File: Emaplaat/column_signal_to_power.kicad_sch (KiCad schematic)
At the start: 56 parts, among them IC3 1EDN7550BXTSA1, IC41 1EDN7550BXTSA1, IC42 1EDN7550BXTSA1, IC43 1EDN7550BXTSA1, IC44 1EDN7550BXTSA1, IC45 1EDN7550BXTSA1, IC46 1EDN7550BXTSA1, IC47 1EDN7550BXTSA1, IC48 1EDN7550BXTSA1, IC49 1EDN7550BXTSA1, IC50 1EDN7550BXTSA1, IC51 1EDN7550BXTSA1, IC52 1EDN7550BXTSA1, IC53 1EDN7550BXTSA1

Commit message: jajald
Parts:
- removed C41, C42, C49, C50, C51, C52, C53, C54, C55, C56, C57, C58: 100u, Capacitor_SMD:C_0201_0603Metric_Pad0.64x0.40mm_HandSolder, symbol Device:C
- added C28, C29, C30, C31, C32, C33, C34, C35, C36, C37, C38, C39: 100u, Capacitor_SMD:C_0603_1608Metric_Pad1.08x0.95mm_HandSolder, symbol Device:C
- C27: renamed from C10; footprint Capacitor_SMD:C_0201_0603Metric_Pad0.64x0.40mm_HandSolder -> Capacitor_SMD:C_0603_1608Metric_Pad1.08x0.95mm_HandSolder
- C40: footprint Capacitor_SMD:C_0201_0603Metric_Pad0.64x0.40mm_HandSolder -> Capacitor_SMD:C_0603_1608Metric_Pad1.08x0.95mm_HandSolder
- renumbered IC3 to IC18, IC44 to IC19, IC50 to IC20, IC41 to IC21, IC45 to IC22, IC51 to IC23, IC42 to IC24, IC46 to IC25, IC52 to IC26, IC43 to IC27, IC48 to IC28, IC53 to IC29, IC47 to IC30, IC49 to IC31, R6 to R27, R64 to R28, R76 to R29, R7 to R30, R65 to R31, R77 to R32, R58 to R33, R66 to R34, R78 to R35, R59 to R36, R67 to R37, R79 to R38, R60 to R39, R68 to R40, R80 to R41, R61 to R42, R69 to R43, R81 to R44, R62 to R45, R72 to R46, R82 to R47, R63 to R48, R73 to R49, R83 to R50, R70 to R51, R74 to R52, R71 to R53, R75 to R54
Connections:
- net 12V: now also C28.2, C29.2, C30.2, C31.2, C32.2, C33.2, C34.2, C35.2, C36.2, C37.2, C38.2, C39.2
- net GND: now also C28.1, C29.1, C30.1, C31.1, C32.1, C33.1, C34.1, C35.1, C36.1, C37.1, C38.1, C39.1

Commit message: skeem korras
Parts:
- IC18, IC19, IC20, IC21, IC22, IC23, IC24, IC25, IC26, IC27, IC28, IC29, IC30, IC31: footprint SOT95P280X145-6N -> SOT95P280X145-6N:SOT95P280X145-6N
- renumbered C36 to C28, C37 to C29, C28 to C30, C35 to C31, C38 to C32, C29 to C33, C39 to C35, C30 to C36, C33 to C37, C40 to C38, C31 to C39, C32 to C40
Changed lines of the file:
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@@
 			)
 		)
-		(property "Footprint" "SOT95P280X145-6N"
+		(property "Footprint" "SOT95P280X145-6N:SOT95P280X145-6N"
 			(at 73.66 258.75 0)
 			(effects
@@
 			)
 		)
-		(property "Footprint" "SOT95P280X145-6N"
+		(property "Footprint" "SOT95P280X145-6N:SOT95P280X145-6N"
 			(at 163.83 126.67 0)
 			(effects
@@
 			)
 		)
-		(property "Footprint" "SOT95P280X145-6N"
+		(property "Footprint" "SOT95P280X145-6N:SOT95P280X145-6N"
 			(at 250.19 229.54 0)
 			(effects
@@
 			)
 		)
-		(property "Footprint" "SOT95P280X145-6N"
+		(property "Footprint" "SOT95P280X145-6N:SOT95P280X145-6N"
 			(at 162.56 162.23 0)
 			(effects
@@
 			)
 		)
-		(property "Footprint" "SOT95P280X145-6N"
+		(property "Footprint" "SOT95P280X145-6N:SOT95P280X145-6N"
 			(at 162.56 228.27 0)
 			(effects
@@
 			)
 		)
-		(property "Footprint" "SOT95P280X145-6N"
+		(property "Footprint" "SOT95P280X145-6N:SOT95P280X145-6N"
 			(at 250.19 196.52 0)
 			(effects
@@
 		(on_board yes)
 		(dnp no)
-		(property "Reference" "C40"
+		(property "Reference" "C38"
 			(at 215.265 143.51 0)
 			(effects
@@
 			(project "Emaplaat"
 				(path "/489224c0-ace1-4530-aa61-a5d03adf1434/1d123e2b-7c0a-4548-ab70-18ecbd0f3e35/07a510d3-c099-46a7-9717-c70cc79e70f4"
-					(reference "C40")
+					(reference "C38")
 					(unit 1)
 				)
@@
 		(on_board yes)
 		(dnp no)
-		(property "Reference" "C37"
+		(property "Reference" "C29"
 			(at 216.535 41.91 0)
 			(effects
@@
 			(project "Emaplaat"
 				(path "/489224c0-ace1-4530-aa61-a5d03adf1434/1d123e2b-7c0a-4548-ab70-18ecbd0f3e35/07a510d3-c099-46a7-9717-c70cc79e70f4"
-					(reference "C37")
+					(reference "C29")
 					(unit 1)
 				)
@@
 		(on_board yes)
 		(dnp no)
-		(property "Reference" "C35"
+		(property "Reference" "C31"
 			(at 127.635 76.2 0)
 			(effects
@@
 			(project "Emaplaat"
 				(path "/489224c0-ace1-4530-aa61-a5d03adf1434/1d123e2b-7c0a-4548-ab70-18ecbd0f3e35/07a510d3-c099-46a7-9717-c70cc79e70f4"
-					(reference "C35")
+					(reference "C31")
 					(unit 1)
 				)
@@
 			)
 		)
-		(property "Footprint" "SOT95P280X145-6N"
+		(property "Footprint" "SOT95P280X145-6N:SOT95P280X145-6N"
 			(at 73.66 191.44 0)
 			(effects
@@
 		(on_board yes)
 		(dnp no)
-		(property "Reference" "C31"
+		(property "Reference" "C39"
 			(at 38.735 172.72 0)
 			(effects
@@
 			(project "Emaplaat"
 				(path "/489224c0-ace1-4530-aa61-a5d03adf1434/1d123e2b-7c0a-4548-ab70-18ecbd0f3e35/07a510d3-c099-46a7-9717-c70cc79e70f4"
-					(reference "C31")
+					(reference "C39")
 					(unit 1)
 				)
@@
 		(on_board yes)
 		(dnp no)
-		(property "Reference" "C38"
+		(property "Reference" "C32"
 			(at 215.265 77.47 0)
 			(effects
@@
 			(project "Emaplaat"
 				(path "/489224c0-ace1-4530-aa61-a5d03adf1434/1d123e2b-7c0a-4548-ab70-18ecbd0f3e35/07a510d3-c099-46a7-9717-c70cc79e70f4"
-					(reference "C38")
+					(reference "C32")
 					(unit 1)
 				)
@@
 			)
 		)
-		(property "Footprint" "SOT95P280X145-6N"
+		(property "Footprint" "SOT95P280X145-6N:SOT95P280X145-6N"
 			(at 162.56 262.56 0)
 			(effects
@@
 		(on_board yes)
 		(dnp no)
-		(property "Reference" "C28"
+		(property "Reference" "C30"
 			(at 38.735 72.39 0)
 			(effects
@@
 			(project "Emaplaat"
 				(path "/489224c0-ace1-4530-aa61-a5d03adf1434/1d123e2b-7c0a-4548-ab70-18ecbd0f3e35/07a510d3-c099-46a7-9717-c70cc79e70f4"
-					(reference "C28")
+					(reference "C30")
 					(unit 1)
 				)
@@
 		(on_board yes)
 		(dnp no)
-		(property "Reference" "C29"
+		(property "Reference" "C33"
 			(at 38.735 105.41 0)
 			(effects
@@
 			(project "Emaplaat"
 				(path "/489224c0-ace1-4530-aa61-a5d03adf1434/1d123e2b-7c0a-4548-ab70-18ecbd0f3e35/07a510d3-c099-46a7-9717-c70cc79e70f4"
-					(reference "C29")
+					(reference "C33")
 					(unit 1)
 				)
@@
 			)
 		)
-		(property "Footprint" "SOT95P280X145-6N"
+		(property "Footprint" "SOT95P280X145-6N:SOT95P280X145-6N"
 			(at 162.56 195.25 0)
 			(effects
@@
 		(on_board yes)
 		(dnp no)
-		(property "Reference" "C39"
+		(property "Reference" "C35"
 			(at 215.265 110.49 0)
 			(effects
@@
 			(project "Emaplaat"
 				(path "/489224c0-ace1-4530-aa61-a5d03adf1434/1d123e2b-7c0a-4548-ab70-18ecbd0f3e35/07a510d3-c099-46a7-9717-c70cc79e70f4"
-					(reference "C39")
+					(reference "C35")
 					(unit 1)
 				)
@@
 			)
 		)
-		(property "Footprint" "SOT95P280X145-6N"
+		(property "Footprint" "SOT95P280X145-6N:SOT95P280X145-6N"
 			(at 73.66 224.46 0)
 			(effects
@@
 			)
 		)
-		(property "Footprint" "SOT95P280X145-6N"
+		(property "Footprint" "SOT95P280X145-6N:SOT95P280X145-6N"
 			(at 250.19 163.5 0)
 			(effects
@@
 		(on_board yes)
 		(dnp no)
-		(property "Reference" "C33"
+		(property "Reference" "C37"
 			(at 127.635 142.24 0)
 			(effects
@@
 			(project "Emaplaat"
 				(path "/489224c0-ace1-4530-aa61-a5d03adf1434/1d123e2b-7c0a-4548-ab70-18ecbd0f3e35/07a510d3-c099-46a7-9717-c70cc79e70f4"
-					(reference "C33")
+					(reference "C37")
 					(unit 1)
 				)
@@
 		(on_board yes)
 		(dnp no)
-		(property "Reference" "C36"
+		(property "Reference" "C28"
 			(at 129.0823 40.64 0)
 			(effects
@@
 			(project "Emaplaat"
 				(path "/489224c0-ace1-4530-aa61-a5d03adf1434/1d123e2b-7c0a-4548-ab70-18ecbd0f3e35/07a510d3-c099-46a7-9717-c70cc79e70f4"
-					(reference "C36")
+					(reference "C28")
 					(unit 1)
 				)
@@
 			)
 		)
-		(property "Footprint" "SOT95P280X145-6N"
+		(property "Footprint" "SOT95P280X145-6N:SOT95P280X145-6N"
 			(at 73.66 158.42 0)
 			(effects
@@
 		(on_board yes)
 		(dnp no)
-		(property "Reference" "C30"
+		(property "Reference" "C36"
 			(at 38.735 138.43 0)
 			(effects
@@
 			(project "Emaplaat"
 				(path "/489224c0-ace1-4530-aa61-a5d03adf1434/1d123e2b-7c0a-4548-ab70-18ecbd0f3e35/07a510d3-c099-46a7-9717-c70cc79e70f4"
-					(reference "C30")
+					(reference "C36")
 					(unit 1)
 				)
@@
 			)
 		)
-		(property "Footprint" "SOT95P280X145-6N"
+		(property "Footprint" "SOT95P280X145-6N:SOT95P280X145-6N"
 			(at 74.93 122.86 0)
 			(effects
@@
 		(on_board yes)
 		(dnp no)
-		(property "Reference" "C32"
+		(property "Reference" "C40"
 			(at 127.635 176.53 0)
 			(effects
@@
 			(project "Emaplaat"
 				(path "/489224c0-ace1-4530-aa61-a5d03adf1434/1d123e2b-7c0a-4548-ab70-18ecbd0f3e35/07a510d3-c099-46a7-9717-c70cc79e70f4"
-					(reference "C32")
+					(reference "C40")
 					(unit 1)
 				)
@@
 			)
 		)
-		(property "Footprint" "SOT95P280X145-6N"
+		(property "Footprint" "SOT95P280X145-6N:SOT95P280X145-6N"
 			(at 251.46 127.94 0)
 			(effects

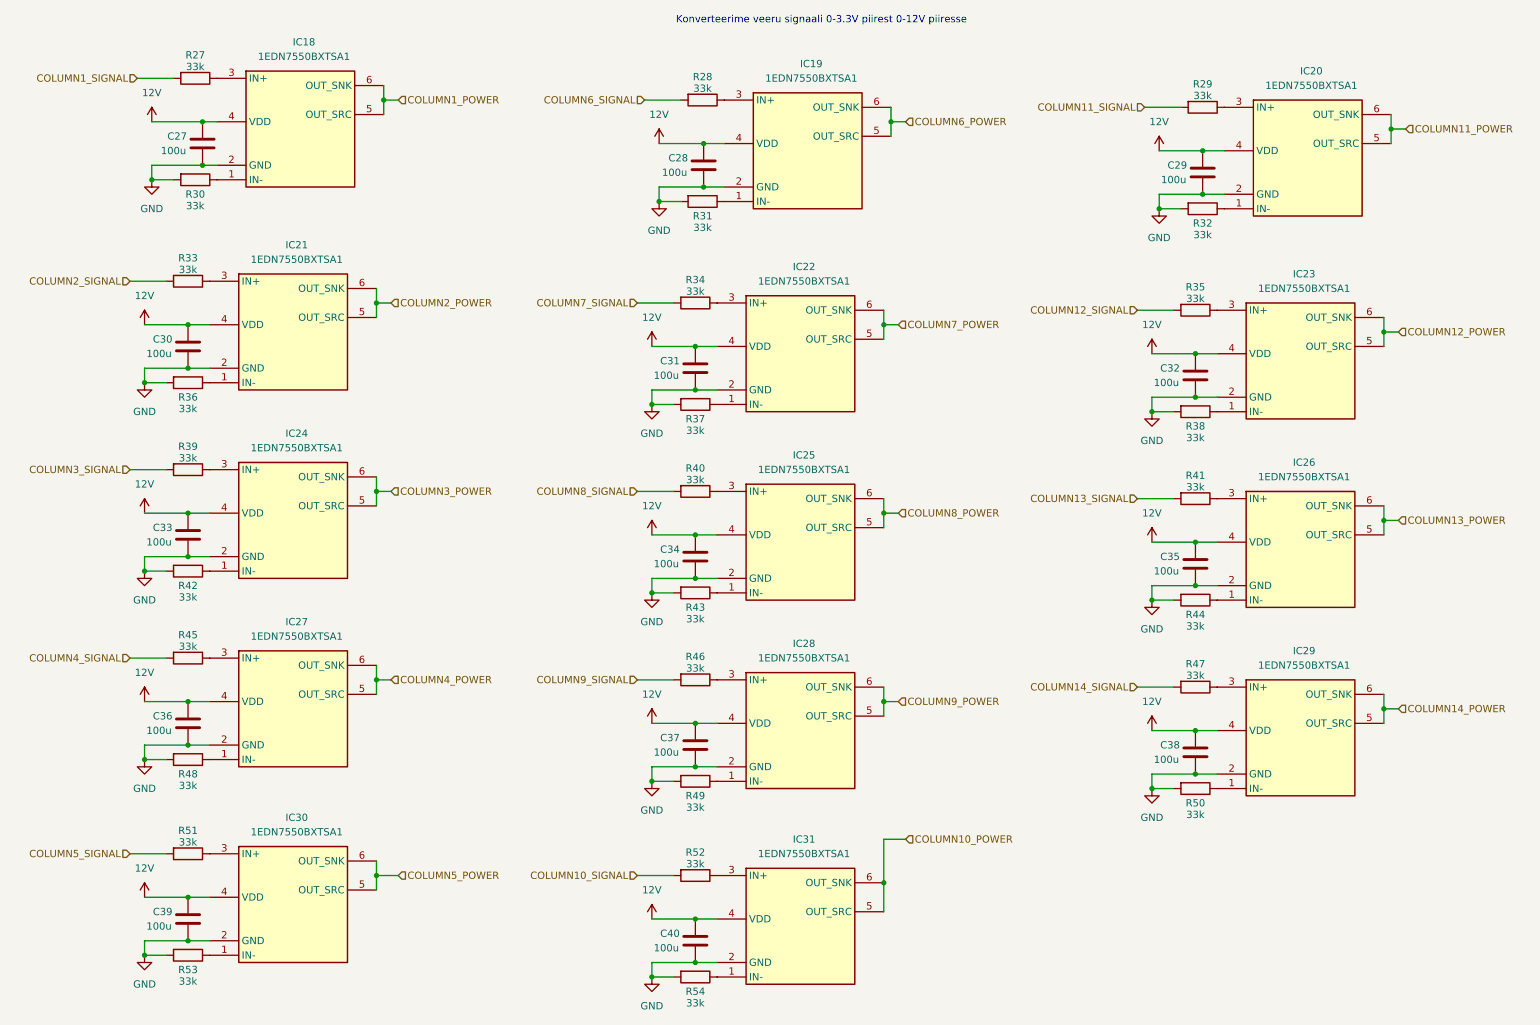
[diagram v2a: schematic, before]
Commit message: Added electrolytic capacitors and 12V rated ESD diode
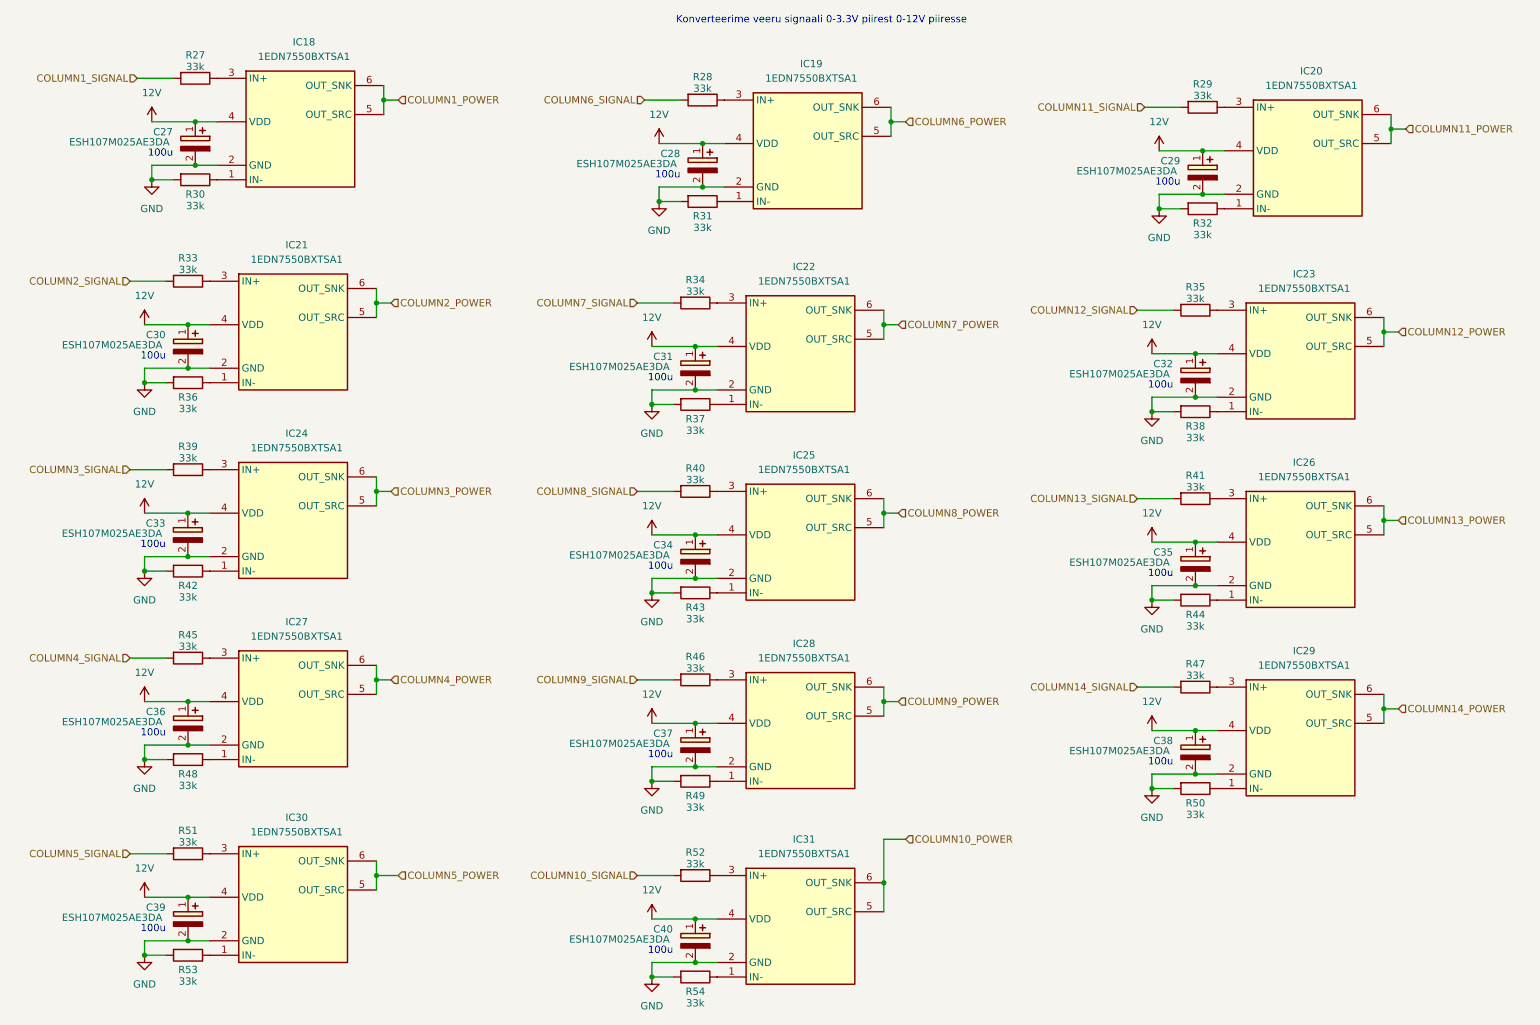
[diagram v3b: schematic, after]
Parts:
- removed C27, C28, C29, C30, C31, C32, C33, C34, C35, C36, C37, C38, C39, C40: 100u, Capacitor_SMD:C_0603_1608Metric_Pad1.08x0.95mm_HandSolder, symbol Device:C
- added C27, C28, C29, C30, C31, C32, C33, C34, C35, C36, C37, C38, C39, C40: ESH107M025AE3DA, CAPPRD250W50D630H1250, symbol ESH107M025AE3DA:ESH107M025AE3DA
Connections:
- net 12V: now also C27.1 (+), C28.1 (+), C29.1 (+), C30.1 (+), C31.1 (+), C32.1 (+), C33.1 (+), C34.1 (+), C35.1 (+), C36.1 (+), C37.1 (+), C38.1 (+), C39.1 (+), C40.1 (+)
- net GND: now also C27.2 (-), C28.2 (-), C29.2 (-), C30.2 (-), C31.2 (-), C32.2 (-), C33.2 (-), C34.2 (-), C35.2 (-), C36.2 (-), C37.2 (-), C38.2 (-), C39.2 (-), C40.2 (-)
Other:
- note added: "100u"
